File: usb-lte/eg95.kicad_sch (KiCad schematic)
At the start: 21 parts, among them J2 Conn_Coaxial, J3 Conn_Coaxial, J4 Conn_Coaxial, U2 EG95

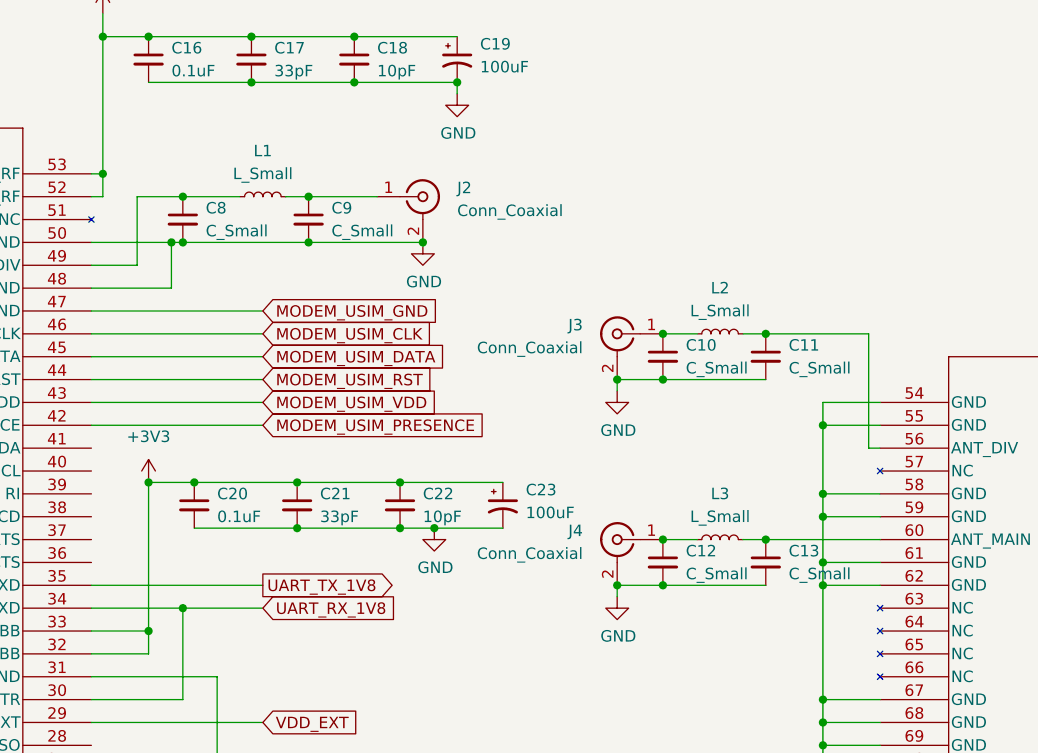
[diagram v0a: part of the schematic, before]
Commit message: Mark pi network caps as NC
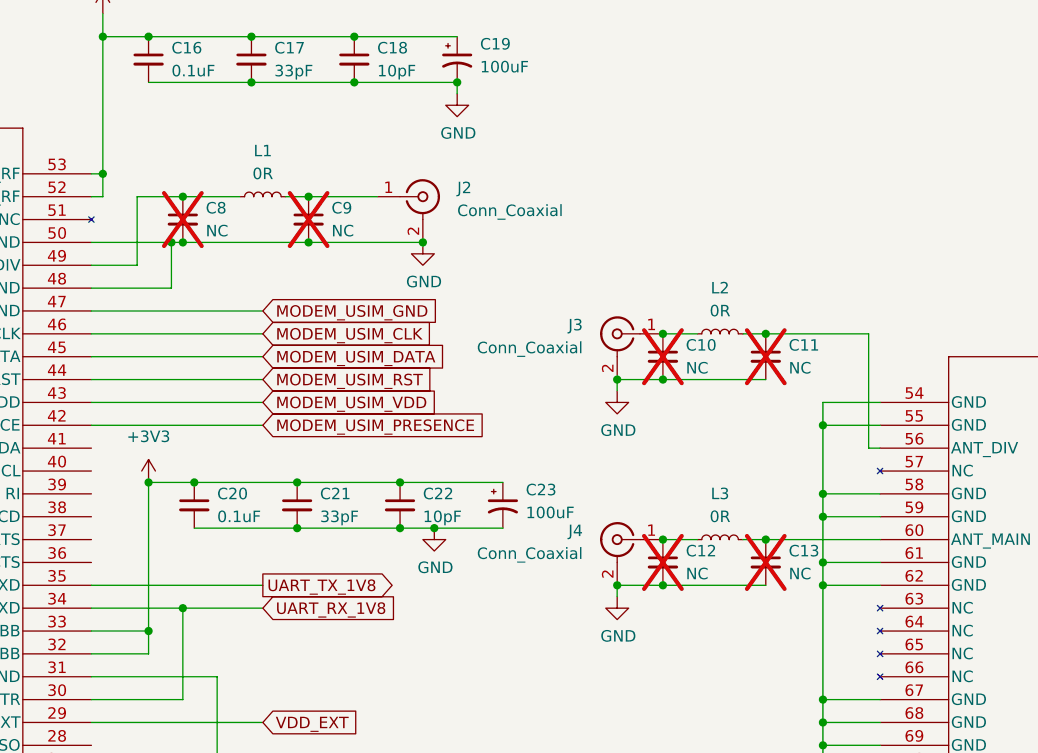
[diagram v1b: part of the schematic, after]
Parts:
- C10, C11, C12, C13, C8, C9: value C_Small -> NC; now not fitted
- L1, L2, L3: value L_Small -> 0R
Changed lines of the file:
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@@
 		(in_bom yes)
 		(on_board yes)
-		(dnp no)
+		(dnp yes)
 		(fields_autoplaced yes)
 		(property "Reference" "C8"
@@
 			)
 		)
-		(property "Value" "C_Small"
+		(property "Value" "NC"
 			(at 123.19 46.9962 0)
 			(effects
@@
 		(in_bom yes)
 		(on_board yes)
-		(dnp no)
+		(dnp yes)
 		(fields_autoplaced yes)
 		(property "Reference" "C10"
@@
 			)
 		)
-		(property "Value" "C_Small"
+		(property "Value" "NC"
 			(at 176.53 62.2362 0)
 			(effects
@@
 			)
 		)
-		(property "Value" "L_Small"
+		(property "Value" "0R"
 			(at 129.54 40.64 90)
 			(effects
@@
 			)
 		)
-		(property "Value" "L_Small"
+		(property "Value" "0R"
 			(at 180.34 78.74 90)
 			(effects
@@
 		(in_bom yes)
 		(on_board yes)
-		(dnp no)
+		(dnp yes)
 		(fields_autoplaced yes)
 		(property "Reference" "C11"
@@
 			)
 		)
-		(property "Value" "C_Small"
+		(property "Value" "NC"
 			(at 187.96 62.2362 0)
 			(effects
@@
 			)
 		)
-		(property "Value" "L_Small"
+		(property "Value" "0R"
 			(at 180.34 55.88 90)
 			(effects
@@
 		(in_bom yes)
 		(on_board yes)
-		(dnp no)
+		(dnp yes)
 		(fields_autoplaced yes)
 		(property "Reference" "C9"
@@
 			)
 		)
-		(property "Value" "C_Small"
+		(property "Value" "NC"
 			(at 137.16 46.9962 0)
 			(effects
@@
 		(in_bom yes)
 		(on_board yes)
-		(dnp no)
+		(dnp yes)
 		(fields_autoplaced yes)
 		(property "Reference" "C13"
@@
 			)
 		)
-		(property "Value" "C_Small"
+		(property "Value" "NC"
 			(at 187.96 85.0962 0)
 			(effects
@@
 		(in_bom yes)
 		(on_board yes)
-		(dnp no)
+		(dnp yes)
 		(fields_autoplaced yes)
 		(property "Reference" "C12"
@@
 			)
 		)
-		(property "Value" "C_Small"
+		(property "Value" "NC"
 			(at 176.53 85.0962 0)
 			(effects

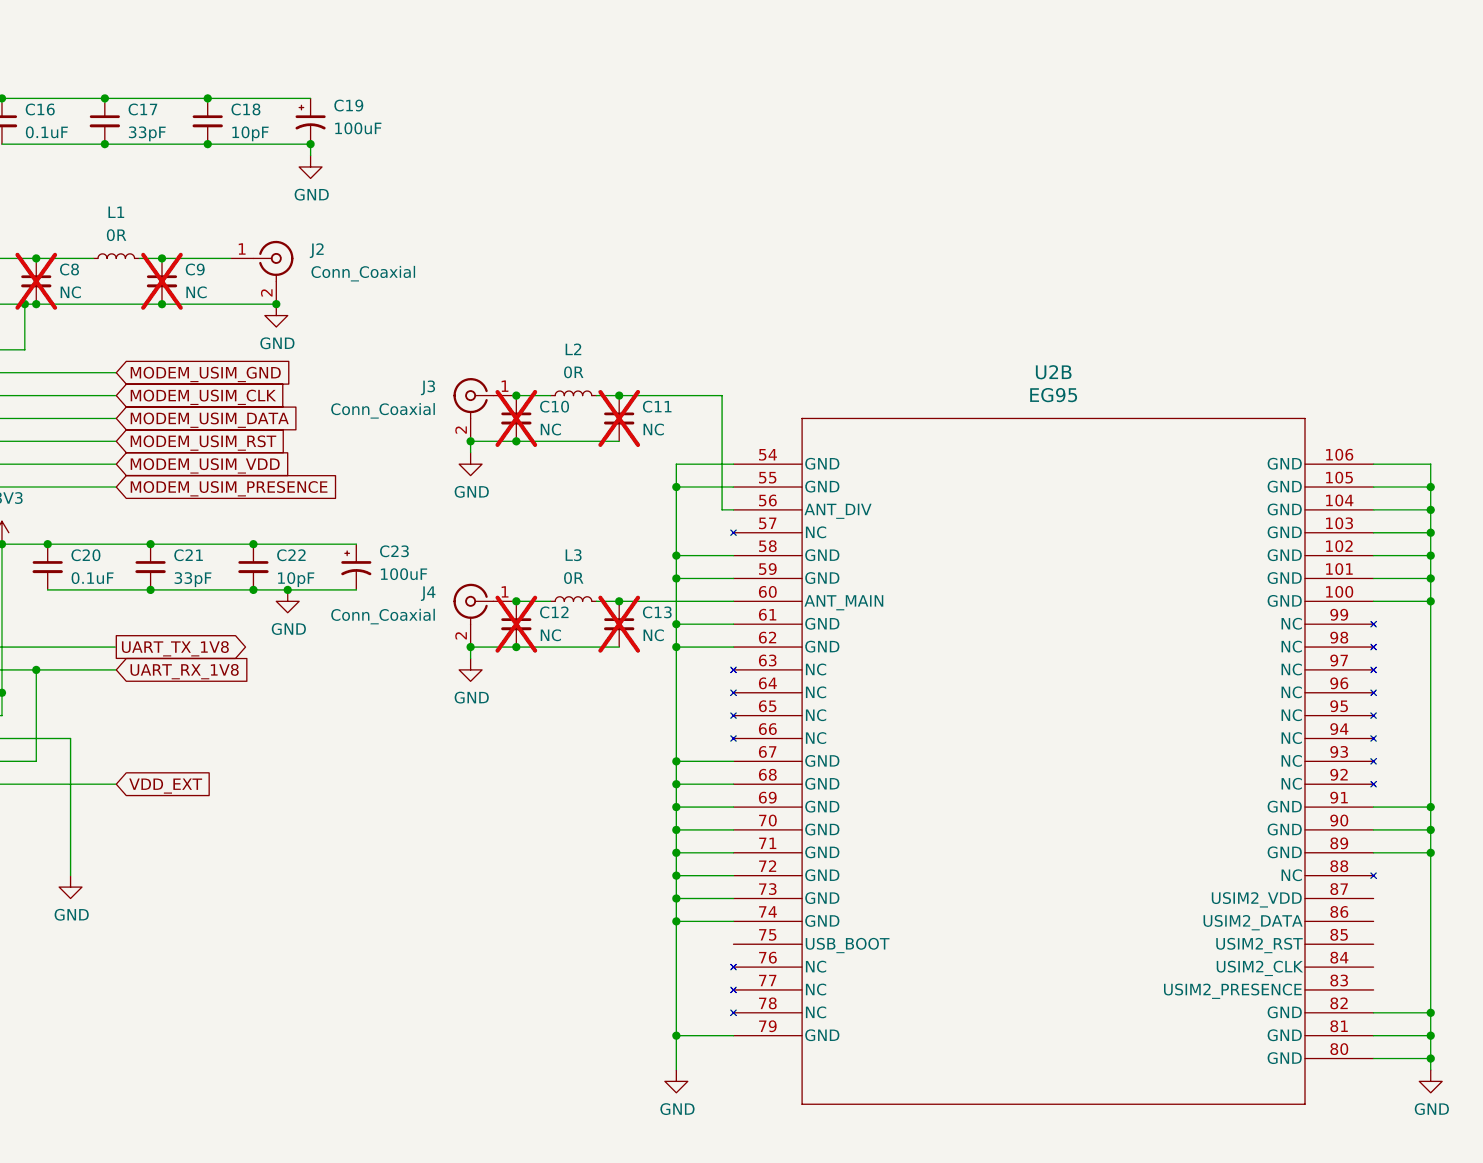
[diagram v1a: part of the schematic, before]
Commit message: Use main power rail for gnss antenna
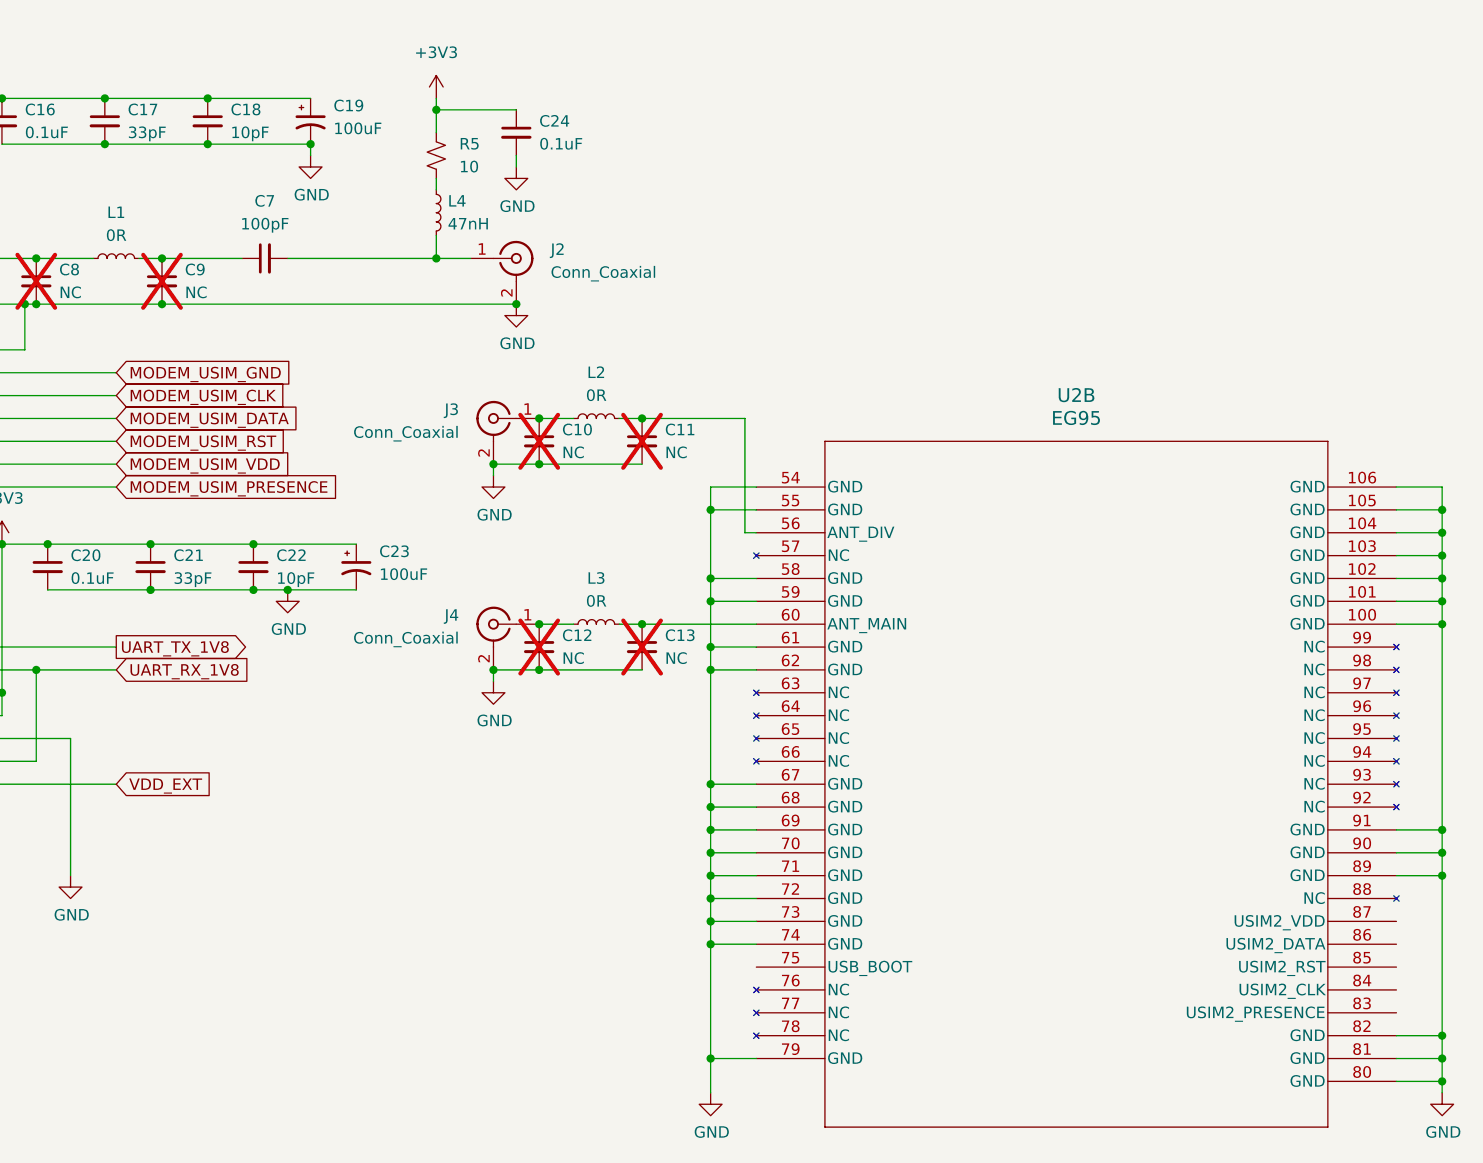
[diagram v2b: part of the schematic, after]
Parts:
- added C24: 0.1uF, Capacitor_SMD:C_0402_1005Metric, symbol Device:C_Small
- added C7: 100pF, Capacitor_SMD:C_0402_1005Metric, symbol Device:C_Small
- added L4: 47nH, Inductor_SMD:L_0402_1005Metric, symbol Device:L_Small
- added R5: 10, Resistor_SMD:R_0402_1005Metric_Pad0.72x0.64mm_HandSolder, symbol Device:R_Small_US
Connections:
- net +3V3: now also C24.1, R5.2
- net GND: now also C24.2
- net at C9.1, L1.2: now also C7.1; no longer J2.1 (In)
- new net: L4.1, R5.1
- new net: C7.2, J2.1 (In), L4.2
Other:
- moved on the sheet: C10, C11, C12, C13, J2, J3, J4, L2, L3, U2B
